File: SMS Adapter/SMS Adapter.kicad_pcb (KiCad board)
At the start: 2 copper layers, 29.2 x 18.4 mm, 4 parts, among them J1 JoyKEY, J2 SMS

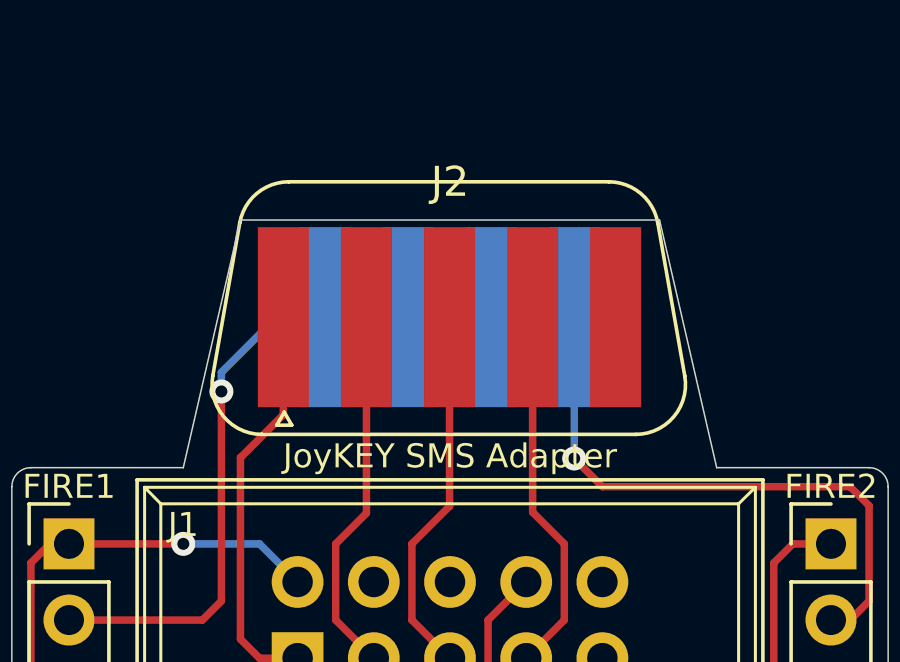
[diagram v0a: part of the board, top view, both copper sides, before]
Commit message: Updated silkscreen
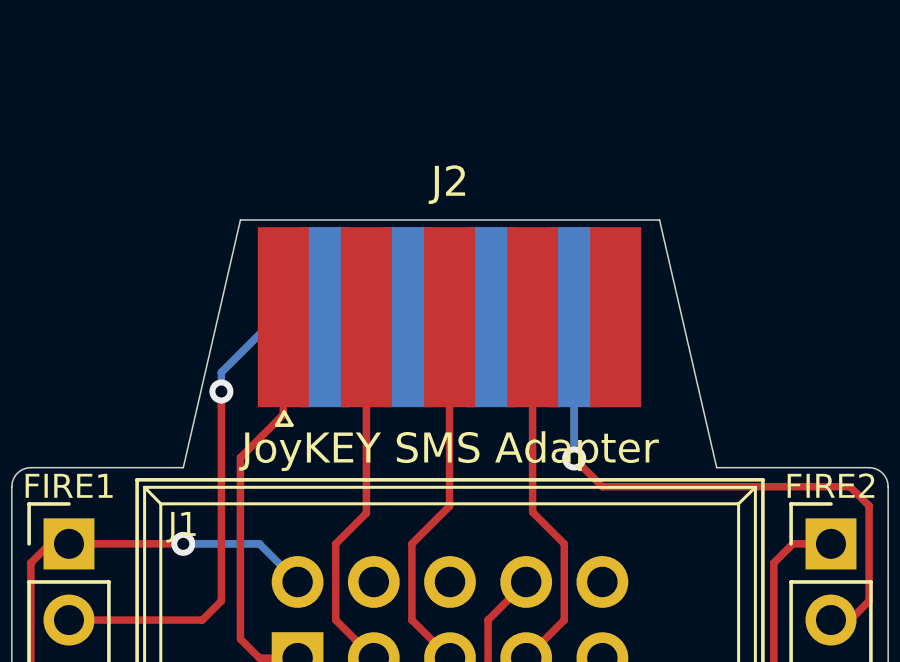
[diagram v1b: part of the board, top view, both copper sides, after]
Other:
- rule pad_to_mask_clearance: 0.051 -> 0
- board text added: "Sega Master System"
